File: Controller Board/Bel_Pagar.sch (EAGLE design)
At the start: 7 parts, among them IC1 7805T, Q1 BD140

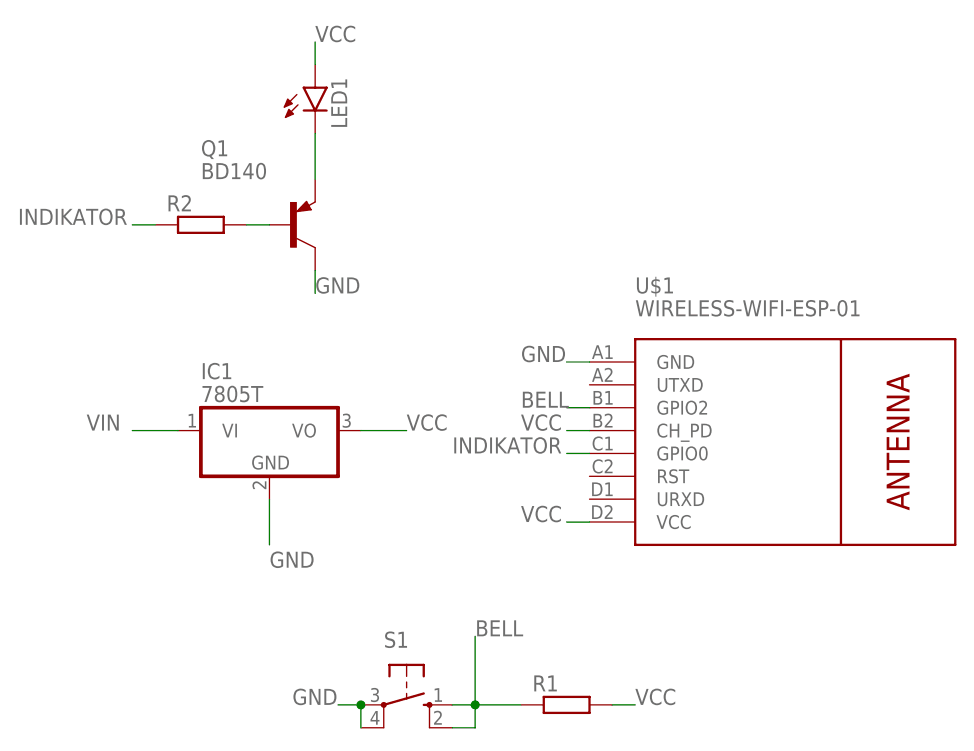
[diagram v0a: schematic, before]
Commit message: Remove 7805 from controller board
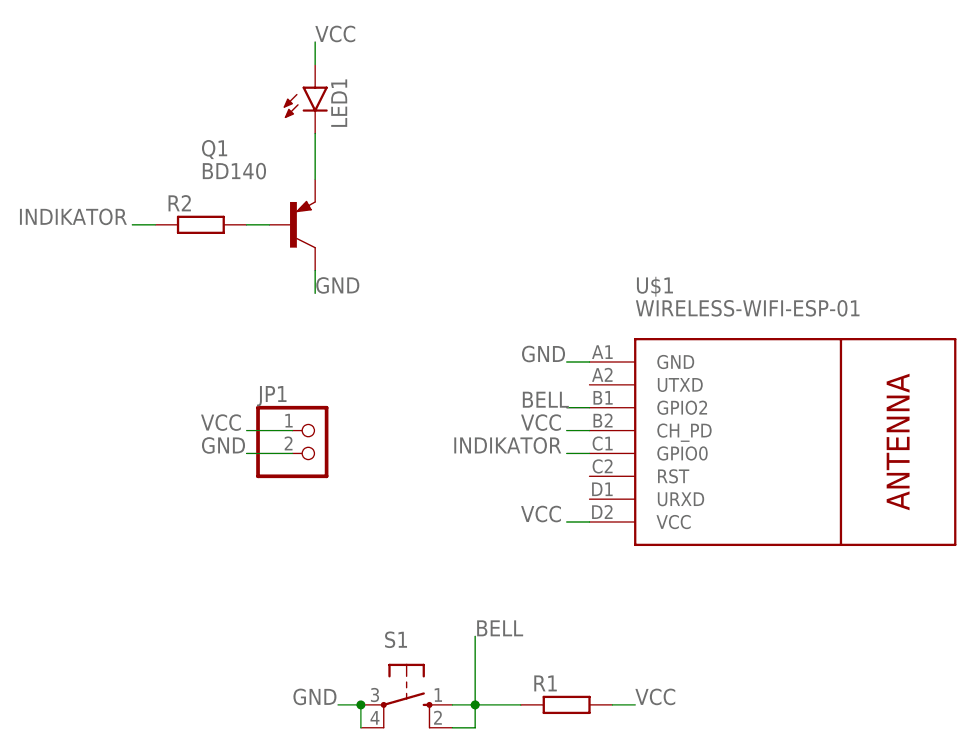
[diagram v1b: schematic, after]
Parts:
- removed IC1: 7805T, linear:7805T
- added JP1: (no value), pinhead:PINHD-1X2
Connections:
- removed net VIN: IC1.VI
- net GND: now also JP1.2; no longer IC1.GND
- net VCC: now also JP1.1; no longer IC1.VO
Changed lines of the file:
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@@
 <part name="U$1" library="diy-modules" deviceset="WIRELESS-WIFI-ESP-01" device=""/>
 <part name="Q1" library="transistor-pnp" library_urn="urn:adsk.eagle:library:399" deviceset="BD140" device="" package3d_urn="urn:adsk.eagle:package:29208/1"/>
-<part name="IC1" library="linear" library_urn="urn:adsk.eagle:library:262" deviceset="78*" device="T" package3d_urn="urn:adsk.eagle:package:16414/1" technology="05"/>
 <part name="S1" library="switch-omron" library_urn="urn:adsk.eagle:library:377" deviceset="10-XX" device="" package3d_urn="urn:adsk.eagle:package:27496/1"/>
 <part name="R1" library="rcl" library_urn="urn:adsk.eagle:library:334" deviceset="R-EU_" device="0207/10" package3d_urn="urn:adsk.eagle:package:23491/2"/>
 <part name="R2" library="rcl" library_urn="urn:adsk.eagle:library:334" deviceset="R-EU_" device="0207/10" package3d_urn="urn:adsk.eagle:package:23491/2"/>
 <part name="LED1" library="led" library_urn="urn:adsk.eagle:library:259" deviceset="LED" device="5MM" package3d_urn="urn:adsk.eagle:package:15799/2"/>
+<part name="JP1" library="pinhead" library_urn="urn:adsk.eagle:library:325" deviceset="PINHD-1X2" device="" package3d_urn="urn:adsk.eagle:package:22435/2"/>
 </parts>
 <sheets>
@@
 <attribute name="NAME" x="-5.08" y="91.44" size="1.778" layer="95"/>
 <attribute name="VALUE" x="-5.08" y="88.9" size="1.778" layer="96"/>
-</instance>
-<instance part="IC1" gate="A1" x="2.54" y="60.96" smashed="yes">
-<attribute name="NAME" x="-5.08" y="66.675" size="1.778" layer="95"/>
-<attribute name="VALUE" x="-5.08" y="64.135" size="1.778" layer="96"/>
 </instance>
 <instance part="S1" gate="1" x="17.78" y="30.48" smashed="yes" rot="R270">
@@
 <attribute name="VALUE" x="13.335" y="94.488" size="1.778" layer="96" rot="R90"/>
 </instance>
+<instance part="JP1" gate="G$1" x="7.62" y="58.42" smashed="yes">
+<attribute name="NAME" x="1.27" y="64.135" size="1.778" layer="95"/>
+<attribute name="VALUE" x="1.27" y="53.34" size="1.778" layer="96"/>
+</instance>
 </instances>
 <busses>
 </busses>
 <nets>
-<net name="VIN" class="0">
-<segment>
-<pinref part="IC1" gate="A1" pin="VI"/>
-<wire x1="-7.62" y1="60.96" x2="-12.7" y2="60.96" width="0.1524" layer="91"/>
-<label x="-17.78" y="60.96" size="1.778" layer="95"/>
-</segment>
-</net>
 <net name="GND" class="0">
-<segment>
-<pinref part="IC1" gate="A1" pin="GND"/>
-<wire x1="2.54" y1="53.34" x2="2.54" y2="48.26" width="0.1524" layer="91"/>
-<label x="2.54" y="45.72" size="1.778" layer="95"/>
-</segment>
 <segment>
 <pinref part="U$1" gate="G$1" pin="GND"/>
@@
 <label x="7.62" y="76.2" size="1.778" layer="95"/>
 </segment>
+<segment>
+<pinref part="JP1" gate="G$1" pin="2"/>
+<wire x1="5.08" y1="58.42" x2="0" y2="58.42" width="0.1524" layer="91"/>
+<label x="-5.08" y="58.42" size="1.778" layer="95"/>
+</segment>
 </net>
 <net name="VCC" class="0">
-<segment>
-<pinref part="IC1" gate="A1" pin="VO"/>
-<wire x1="12.7" y1="60.96" x2="17.78" y2="60.96" width="0.1524" layer="91"/>
-<label x="17.78" y="60.96" size="1.778" layer="95"/>
-</segment>
 <segment>
 <pinref part="U$1" gate="G$1" pin="VCC"/>
@@
 <label x="7.62" y="104.14" size="1.778" layer="95"/>
 </segment>
+<segment>
+<pinref part="JP1" gate="G$1" pin="1"/>
+<wire x1="5.08" y1="60.96" x2="0" y2="60.96" width="0.1524" layer="91"/>
+<label x="-5.08" y="60.96" size="1.778" layer="95"/>
+</segment>
 </net>
